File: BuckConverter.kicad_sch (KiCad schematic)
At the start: 8 parts, among them U1 TPS62133, U2 APH0630T2R2M

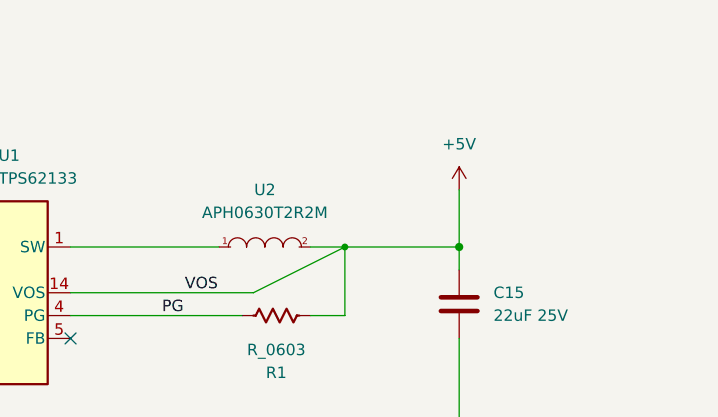
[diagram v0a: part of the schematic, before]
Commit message: etiquetar cables
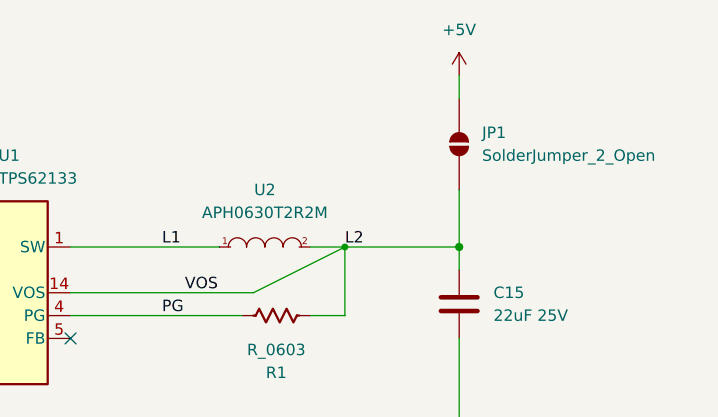
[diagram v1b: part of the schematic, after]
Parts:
- added JP1: SolderJumper_2_Open, symbol Jumper:SolderJumper_2_Open
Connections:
- net +5V: now also JP1.2 (B); no longer C15.1, R1.1, U1.14 (VOS), U2.2
- net L1: now reaches U1.1 (SW), U1.2 (SW), U1.3 (SW), U2.1
- new net L2: C15.1, JP1.1 (A), R1.1, U1.14 (VOS), U2.2
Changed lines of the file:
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@@
 	(wire
 		(pts
-			(xy 259.08 91.44) (xy 255.27 91.44)
+			(xy 255.27 91.44) (xy 271.78 91.44)
 		)
 		(stroke
@@
 	(wire
 		(pts
-			(xy 271.78 91.44) (xy 259.08 91.44)
-		)
-		(stroke
-			(width 0.508)
-			(type default)
-		)
-	)
-	(wire
-		(pts
 			(xy 185.42 93.98) (xy 208.28 93.98)
+		)
+		(stroke
+			(width 0)
+			(type default)
+		)
+	)
+	(wire
+		(pts
+			(xy 271.78 72.39) (xy 271.78 74.93)
 		)
 		(stroke
@@
 		)
 	)
+	(label "L2"
+		(at 259.08 91.44 0)
+		(effects
+			(font
+				(size 1.27 1.27)
+			)
+			(justify left bottom)
+		)
+	)
 	(label "EN_BUCK"
 		(at 186.69 91.44 0)
+		(effects
+			(font
+				(size 1.27 1.27)
+			)
+			(justify left bottom)
+		)
+	)
+	(label "L1"
+		(at 238.76 91.44 0)
 		(effects
 			(font
@@
 	)
 	(symbol
+		(lib_id "power:+5V")
+		(at 271.78 72.39 0)
+		(unit 1)
+		(body_style 1)
+		(exclude_from_sim no)
+		(in_bom yes)
+		(on_board yes)
+		(in_pos_files yes)
+		(dnp no)
+		(fields_autoplaced yes)
+		(property "Reference" "#PWR03"
+			(at 271.78 76.2 0)
+			(hide yes)
+			(show_name no)
+			(do_not_autoplace no)
+			(effects
+				(font
+					(size 1.27 1.27)
+				)
+			)
+		)
+		(property "Value" "+5V"
+			(at 271.78 67.31 0)
+			(show_name no)
+			(do_not_autoplace no)
+			(effects
+				(font
+					(size 1.27 1.27)
+				)
+			)
+		)
+		(property "Footprint" ""
+			(at 271.78 72.39 0)
+			(hide yes)
+			(show_name no)
+			(do_not_autoplace no)
+			(effects
+				(font
+					(size 1.27 1.27)
+				)
+			)
+		)
+		(property "Datasheet" ""
+			(at 271.78 72.39 0)
+			(hide yes)
+			(show_name no)
+			(do_not_autoplace no)
+			(effects
+				(font
+					(size 1.27 1.27)
+				)
+			)
+		)
+		(property "Description" "Power symbol creates a global label with name \"+5V\""
+			(at 271.78 72.39 0)
+			(hide yes)
+			(show_name no)
+			(do_not_autoplace no)
+			(effects
+				(font
+					(size 1.27 1.27)
+				)
+			)
+		)
+		(pin "1"
+		)
+		(instances
+			(project "USAR_Drone_Feature"
+				(path "/b3437995-bb94-4c2f-9ed8-b1af477fe956/c7355bec-9410-4168-a517-83785ccd3002"
+					(reference "#PWR03")
+					(unit 1)
+				)
+			)
+		)
+	)
+	(symbol
 		(lib_id "Regulator_Switching:TPS62133")
 		(at 218.44 96.52 0)
@@
 				(path "/b3437995-bb94-4c2f-9ed8-b1af477fe956/c7355bec-9410-4168-a517-83785ccd3002"
 					(reference "U1")
-					(unit 1)
-				)
-			)
-		)
-	)
-	(symbol
-		(lib_id "power:+5V")
-		(at 271.78 85.09 0)
-		(unit 1)
-		(body_style 1)
-		(exclude_from_sim no)
-		(in_bom yes)
-		(on_board yes)
-		(in_pos_files yes)
-		(dnp no)
-		(fields_autoplaced yes)
-		(property "Reference" "#PWR03"
-			(at 271.78 88.9 0)
-			(hide yes)
-			(show_name no)
-			(do_not_autoplace no)
-			(effects
-				(font
-					(size 1.27 1.27)
-				)
-			)
-		)
-		(property "Value" "+5V"
-			(at 271.78 80.01 0)
-			(show_name no)
-			(do_not_autoplace no)
-			(effects
-				(font
-					(size 1.27 1.27)
-				)
-			)
-		)
-		(property "Footprint" ""
-			(at 271.78 85.09 0)
-			(hide yes)
-			(show_name no)
-			(do_not_autoplace no)
-			(effects
-				(font
-					(size 1.27 1.27)
-				)
-			)
-		)
-		(property "Datasheet" ""
-			(at 271.78 85.09 0)
-			(hide yes)
-			(show_name no)
-			(do_not_autoplace no)
-			(effects
-				(font
-					(size 1.27 1.27)
-				)
-			)
-		)
-		(property "Description" "Power symbol creates a global label with name \"+5V\""
-			(at 271.78 85.09 0)
-			(hide yes)
-			(show_name no)
-			(do_not_autoplace no)
-			(effects
-				(font
-					(size 1.27 1.27)
-				)
-			)
-		)
-		(pin "1"
-		)
-		(instances
-			(project "USAR_Drone_Feature"
-				(path "/b3437995-bb94-4c2f-9ed8-b1af477fe956/c7355bec-9410-4168-a517-83785ccd3002"
-					(reference "#PWR03")
 					(unit 1)
 				)
@@
 					(unit 1)
 				)
+			)
+		)
+	)
+	(symbol
+		(lib_id "Jumper:SolderJumper_2_Open")
+		(at 271.78 80.01 90)
+		(unit 1)
+		(body_style 1)
+		(exclude_from_sim no)
+		(in_bom no)
+		(on_board yes)
+		(in_pos_files yes)
+		(dnp no)
+		(fields_autoplaced yes)
+		(property "Reference" "JP1"
+			(at 274.32 78.7399 90)
+			(show_name no)
+			(do_not_autoplace no)
+			(effects
+				(font
+					(size 1.27 1.27)
+				)
+				(justify right)
+			)
+		)
+		(property "Value" "SolderJumper_2_Open"
+			(at 274.32 81.2799 90)
+			(show_name no)
+			(do_not_autoplace no)
+			(effects
+				(font
+					(size 1.27 1.27)
+				)
+				(justify right)
+			)
+		)
+		(property "Footprint" ""
+			(at 271.78 80.01 0)
+			(hide yes)
+			(show_name no)
+			(do_not_autoplace no)
+			(effects
+				(font
+					(size 1.27 1.27)
+				)
+			)
+		)
+		(property "Datasheet" ""
+			(at 279.4 80.01 0)
+			(hide yes)
+			(show_name no)
+			(do_not_autoplace no)
+			(effects
+				(font
+					(size 1.27 1.27)
+				)
+			)
+		)
+		(property "Description" "Solder Jumper, 2-pole, open"
+			(at 276.86 80.01 0)
+			(hide yes)
+			(show_name no)
+			(do_not_autoplace no)
+			(effects
+				(font
+					(size 1.27 1.27)
+				)
+			)
+		)
+		(pin "1"
+		)
+		(pin "2"
+		)
+		(instances
+			(project "USAR_Drone_Feature"
+				(path "/b3437995-bb94-4c2f-9ed8-b1af477fe956/c7355bec-9410-4168-a517-83785ccd3002"
+					(reference "JP1")
+					(unit 1)
+				)

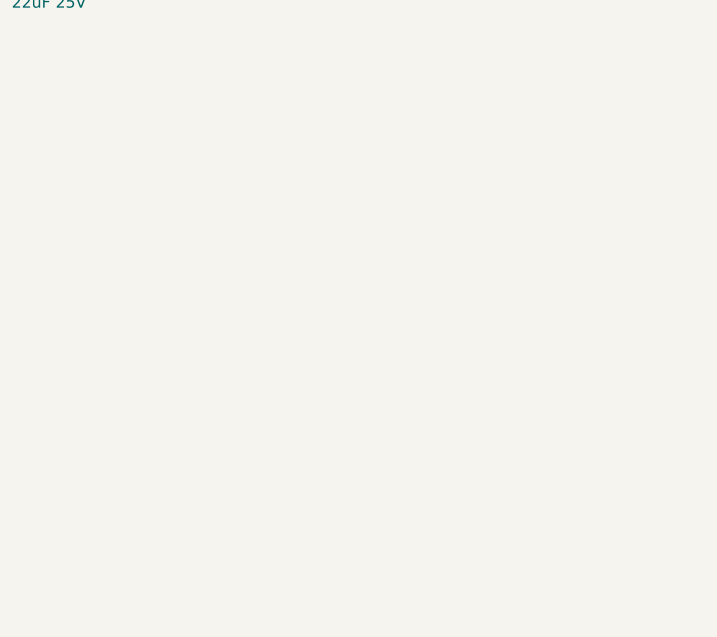
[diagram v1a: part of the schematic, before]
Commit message: add LDO 3v3, change buckconverter sheet to Power Rails
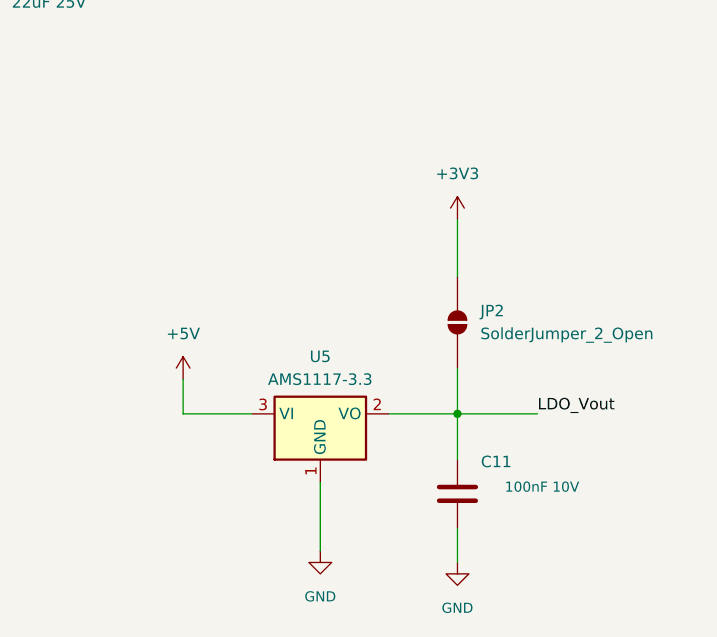
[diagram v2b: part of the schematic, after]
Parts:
- added C11: 100nF 10V, PCM_Capacitor_SMD_AKL:C_0603_1608Metric, symbol PCM_Capacitor_US_AKL:C_0603
- added JP2: SolderJumper_2_Open, symbol Jumper:SolderJumper_2_Open
- added U5: AMS1117-3.3, Package_TO_SOT_SMD:SOT-223-3_TabPin2, symbol Regulator_Linear:AMS1117-3.3
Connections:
- net +5V: now also U5.3 (VI)
- net GND: now also C11.2, U5.1 (GND)
- new net +3V3: JP2.2 (B)
- new net LDO_Vout: C11.1, JP2.1 (A), U5.2 (VO)

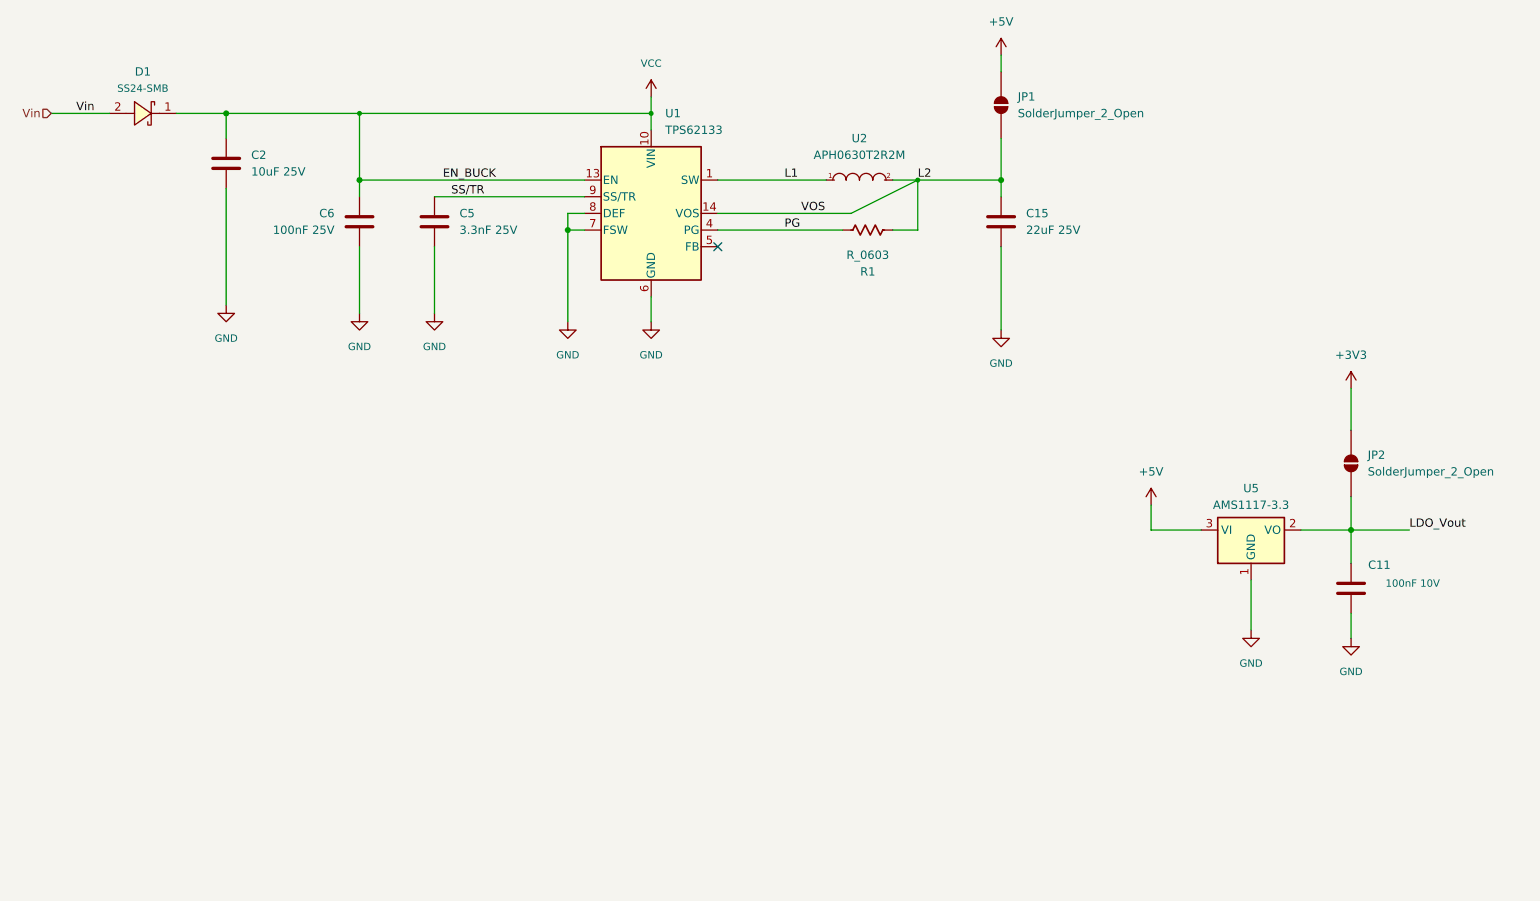
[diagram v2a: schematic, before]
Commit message: modificacion general de esquematico
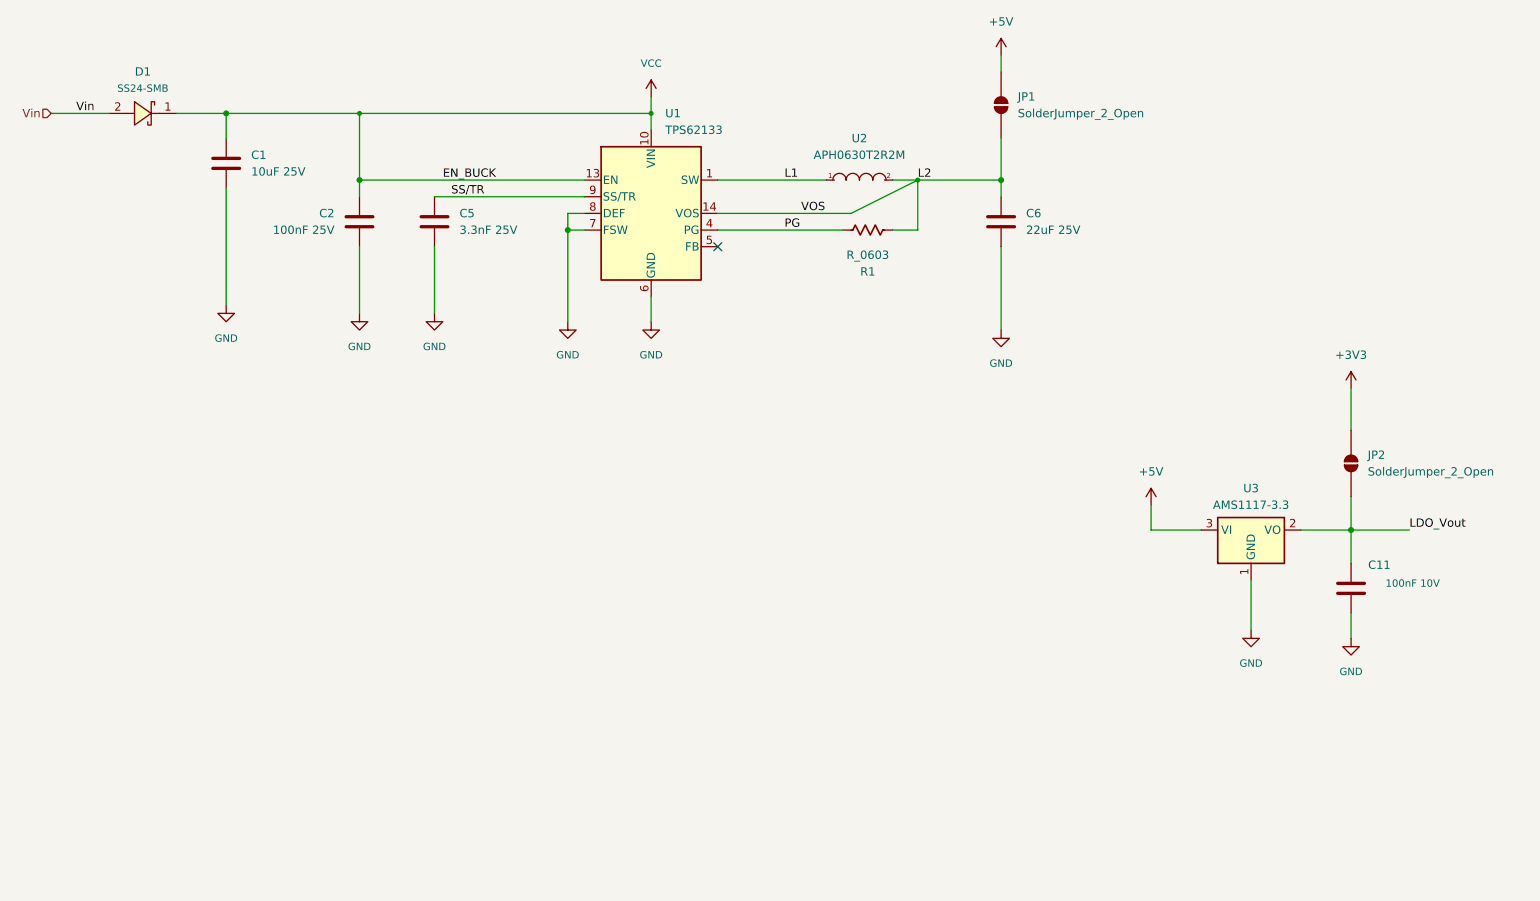
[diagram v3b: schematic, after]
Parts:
- renumbered C2 to C1, C6 to C2, C15 to C6, U5 to U3
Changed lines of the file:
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@@
 		(instances
 			(project "USAR_Drone_Feature"
-				(path "/b3437995-bb94-4c2f-9ed8-b1af477fe956/c7355bec-9410-4168-a517-83785ccd3002"
+				(path "/b3437995-bb94-4c2f-9ed8-b1af477fe956/bbae36a6-1608-41fb-8b94-fa07ee9e7141"
 					(reference "#PWR011")
 					(unit 1)
@@
 		(instances
 			(project "USAR_Drone_Feature"
-				(path "/b3437995-bb94-4c2f-9ed8-b1af477fe956/c7355bec-9410-4168-a517-83785ccd3002"
+				(path "/b3437995-bb94-4c2f-9ed8-b1af477fe956/bbae36a6-1608-41fb-8b94-fa07ee9e7141"
 					(reference "#PWR07")
 					(unit 1)
@@
 		(instances
 			(project "USAR_Drone_Feature"
-				(path "/b3437995-bb94-4c2f-9ed8-b1af477fe956/c7355bec-9410-4168-a517-83785ccd3002"
+				(path "/b3437995-bb94-4c2f-9ed8-b1af477fe956/bbae36a6-1608-41fb-8b94-fa07ee9e7141"
 					(reference "C11")
 					(unit 1)
@@
 		(instances
 			(project "USAR_Drone_Feature"
-				(path "/b3437995-bb94-4c2f-9ed8-b1af477fe956/c7355bec-9410-4168-a517-83785ccd3002"
+				(path "/b3437995-bb94-4c2f-9ed8-b1af477fe956/bbae36a6-1608-41fb-8b94-fa07ee9e7141"
 					(reference "#PWR019")
 					(unit 1)
@@
 		(in_pos_files yes)
 		(dnp no)
-		(property "Reference" "C6"
+		(property "Reference" "C2"
 			(at 170.18 96.5199 0)
 			(show_name no)
@@
 		(instances
 			(project "USAR_Drone_Feature"
-				(path "/b3437995-bb94-4c2f-9ed8-b1af477fe956/c7355bec-9410-4168-a517-83785ccd3002"
-					(reference "C6")
+				(path "/b3437995-bb94-4c2f-9ed8-b1af477fe956/bbae36a6-1608-41fb-8b94-fa07ee9e7141"
+					(reference "C2")
 					(unit 1)
 				)
@@
 		(instances
 			(project "USAR_Drone_Feature"
-				(path "/b3437995-bb94-4c2f-9ed8-b1af477fe956/c7355bec-9410-4168-a517-83785ccd3002"
+				(path "/b3437995-bb94-4c2f-9ed8-b1af477fe956/bbae36a6-1608-41fb-8b94-fa07ee9e7141"
 					(reference "D1")
 					(unit 1)
@@
 		(instances
 			(project "USAR_Drone_Feature"
-				(path "/b3437995-bb94-4c2f-9ed8-b1af477fe956/c7355bec-9410-4168-a517-83785ccd3002"
+				(path "/b3437995-bb94-4c2f-9ed8-b1af477fe956/bbae36a6-1608-41fb-8b94-fa07ee9e7141"
 					(reference "#PWR06")
 					(unit 1)
@@
 		(dnp no)
 		(fields_autoplaced yes)
-		(property "Reference" "U5"
+		(property "Reference" "U3"
 			(at 309.88 138.43 0)
 			(show_name no)
@@
 		(instances
 			(project "USAR_Drone_Feature"
-				(path "/b3437995-bb94-4c2f-9ed8-b1af477fe956/c7355bec-9410-4168-a517-83785ccd3002"
-					(reference "U5")
+				(path "/b3437995-bb94-4c2f-9ed8-b1af477fe956/bbae36a6-1608-41fb-8b94-fa07ee9e7141"
+					(reference "U3")
 					(unit 1)
 				)
@@
 		(instances
 			(project "USAR_Drone_Feature"
-				(path "/b3437995-bb94-4c2f-9ed8-b1af477fe956/c7355bec-9410-4168-a517-83785ccd3002"
+				(path "/b3437995-bb94-4c2f-9ed8-b1af477fe956/bbae36a6-1608-41fb-8b94-fa07ee9e7141"
 					(reference "#PWR020")
 					(unit 1)
@@
 		(instances
 			(project "USAR_Drone_Feature"
-				(path "/b3437995-bb94-4c2f-9ed8-b1af477fe956/c7355bec-9410-4168-a517-83785ccd3002"
+				(path "/b3437995-bb94-4c2f-9ed8-b1af477fe956/bbae36a6-1608-41fb-8b94-fa07ee9e7141"
 					(reference "R1")
 					(unit 1)
@@
 		(instances
 			(project "USAR_Drone_Feature"
-				(path "/b3437995-bb94-4c2f-9ed8-b1af477fe956/c7355bec-9410-4168-a517-83785ccd3002"
+				(path "/b3437995-bb94-4c2f-9ed8-b1af477fe956/bbae36a6-1608-41fb-8b94-fa07ee9e7141"
 					(reference "#PWR014")
 					(unit 1)
@@
 		(instances
 			(project "USAR_Drone_Feature"
-				(path "/b3437995-bb94-4c2f-9ed8-b1af477fe956/c7355bec-9410-4168-a517-83785ccd3002"
+				(path "/b3437995-bb94-4c2f-9ed8-b1af477fe956/bbae36a6-1608-41fb-8b94-fa07ee9e7141"
 					(reference "#PWR018")
 					(unit 1)
@@
 		(instances
 			(project "USAR_Drone_Feature"
-				(path "/b3437995-bb94-4c2f-9ed8-b1af477fe956/c7355bec-9410-4168-a517-83785ccd3002"
+				(path "/b3437995-bb94-4c2f-9ed8-b1af477fe956/bbae36a6-1608-41fb-8b94-fa07ee9e7141"
 					(reference "#PWR016")
 					(unit 1)
@@
 		(instances
 			(project "USAR_Drone_Feature"
-				(path "/b3437995-bb94-4c2f-9ed8-b1af477fe956/c7355bec-9410-4168-a517-83785ccd3002"
+				(path "/b3437995-bb94-4c2f-9ed8-b1af477fe956/bbae36a6-1608-41fb-8b94-fa07ee9e7141"
 					(reference "#PWR017")
 					(unit 1)
@@
 		(instances
 			(project "USAR_Drone_Feature"
-				(path "/b3437995-bb94-4c2f-9ed8-b1af477fe956/c7355bec-9410-4168-a517-83785ccd3002"
+				(path "/b3437995-bb94-4c2f-9ed8-b1af477fe956/bbae36a6-1608-41fb-8b94-fa07ee9e7141"
 					(reference "#PWR03")
 					(unit 1)
@@
 		(instances
 			(project "USAR_Drone_Feature"
-				(path "/b3437995-bb94-4c2f-9ed8-b1af477fe956/c7355bec-9410-4168-a517-83785ccd3002"
+				(path "/b3437995-bb94-4c2f-9ed8-b1af477fe956/bbae36a6-1608-41fb-8b94-fa07ee9e7141"
 					(reference "U1")
 					(unit 1)
@@
 		(instances
 			(project "USAR_Drone_Feature"
-				(path "/b3437995-bb94-4c2f-9ed8-b1af477fe956/c7355bec-9410-4168-a517-83785ccd3002"
+				(path "/b3437995-bb94-4c2f-9ed8-b1af477fe956/bbae36a6-1608-41fb-8b94-fa07ee9e7141"
 					(reference "#PWR05")
 					(unit 1)
@@
 		(instances
 			(project "USAR_Drone_Feature"
-				(path "/b3437995-bb94-4c2f-9ed8-b1af477fe956/c7355bec-9410-4168-a517-83785ccd3002"
+				(path "/b3437995-bb94-4c2f-9ed8-b1af477fe956/bbae36a6-1608-41fb-8b94-fa07ee9e7141"
 					(reference "#PWR013")
 					(unit 1)
@@
 		(dnp no)
 		(fields_autoplaced yes)
-		(property "Reference" "C15"
+		(property "Reference" "C6"
 			(at 275.59 96.5199 0)
 			(show_name no)
@@
 		(instances
 			(project "USAR_Drone_Feature"
-				(path "/b3437995-bb94-4c2f-9ed8-b1af477fe956/c7355bec-9410-4168-a517-83785ccd3002"
-					(reference "C15")
+				(path "/b3437995-bb94-4c2f-9ed8-b1af477fe956/bbae36a6-1608-41fb-8b94-fa07ee9e7141"
+					(reference "C6")
 					(unit 1)
 				)
@@
 		(dnp no)
 		(fields_autoplaced yes)
-		(property "Reference" "C2"
+		(property "Reference" "C1"
 			(at 157.48 87.6299 0)
 			(show_name no)
@@
 		(instances
 			(project "USAR_Drone_Feature"
-				(path "/b3437995-bb94-4c2f-9ed8-b1af477fe956/c7355bec-9410-4168-a517-83785ccd3002"
-					(reference "C2")
+				(path "/b3437995-bb94-4c2f-9ed8-b1af477fe956/bbae36a6-1608-41fb-8b94-fa07ee9e7141"
+					(reference "C1")
 					(unit 1)
 				)
@@
 		(instances
 			(project "USAR_Drone_Feature"
-				(path "/b3437995-bb94-4c2f-9ed8-b1af477fe956/c7355bec-9410-4168-a517-83785ccd3002"
+				(path "/b3437995-bb94-4c2f-9ed8-b1af477fe956/bbae36a6-1608-41fb-8b94-fa07ee9e7141"
 					(reference "JP1")
 					(unit 1)
@@
 		(instances
 			(project "USAR_Drone_Feature"
-				(path "/b3437995-bb94-4c2f-9ed8-b1af477fe956/c7355bec-9410-4168-a517-83785ccd3002"
+				(path "/b3437995-bb94-4c2f-9ed8-b1af477fe956/bbae36a6-1608-41fb-8b94-fa07ee9e7141"
 					(reference "C5")
 					(unit 1)
@@
 		(instances
 			(project "USAR_Drone_Feature"
-				(path "/b3437995-bb94-4c2f-9ed8-b1af477fe956/c7355bec-9410-4168-a517-83785ccd3002"
+				(path "/b3437995-bb94-4c2f-9ed8-b1af477fe956/bbae36a6-1608-41fb-8b94-fa07ee9e7141"
 					(reference "JP2")
 					(unit 1)
@@
 		(instances
 			(project "USAR_Drone_Feature"
-				(path "/b3437995-bb94-4c2f-9ed8-b1af477fe956/c7355bec-9410-4168-a517-83785ccd3002"
+				(path "/b3437995-bb94-4c2f-9ed8-b1af477fe956/bbae36a6-1608-41fb-8b94-fa07ee9e7141"
 					(reference "U2")
 					(unit 1)
